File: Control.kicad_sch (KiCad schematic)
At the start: 8 parts, among them U1 XC95144XL-TQ100

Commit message: more
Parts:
- removed U1: XC95144XL-TQ100, stdpads:TQFP-100_14x14mm_P0.5mm, symbol CPLD_Xilinx:XC95144XL-TQ100
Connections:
- no-connect marks 2 -> 0

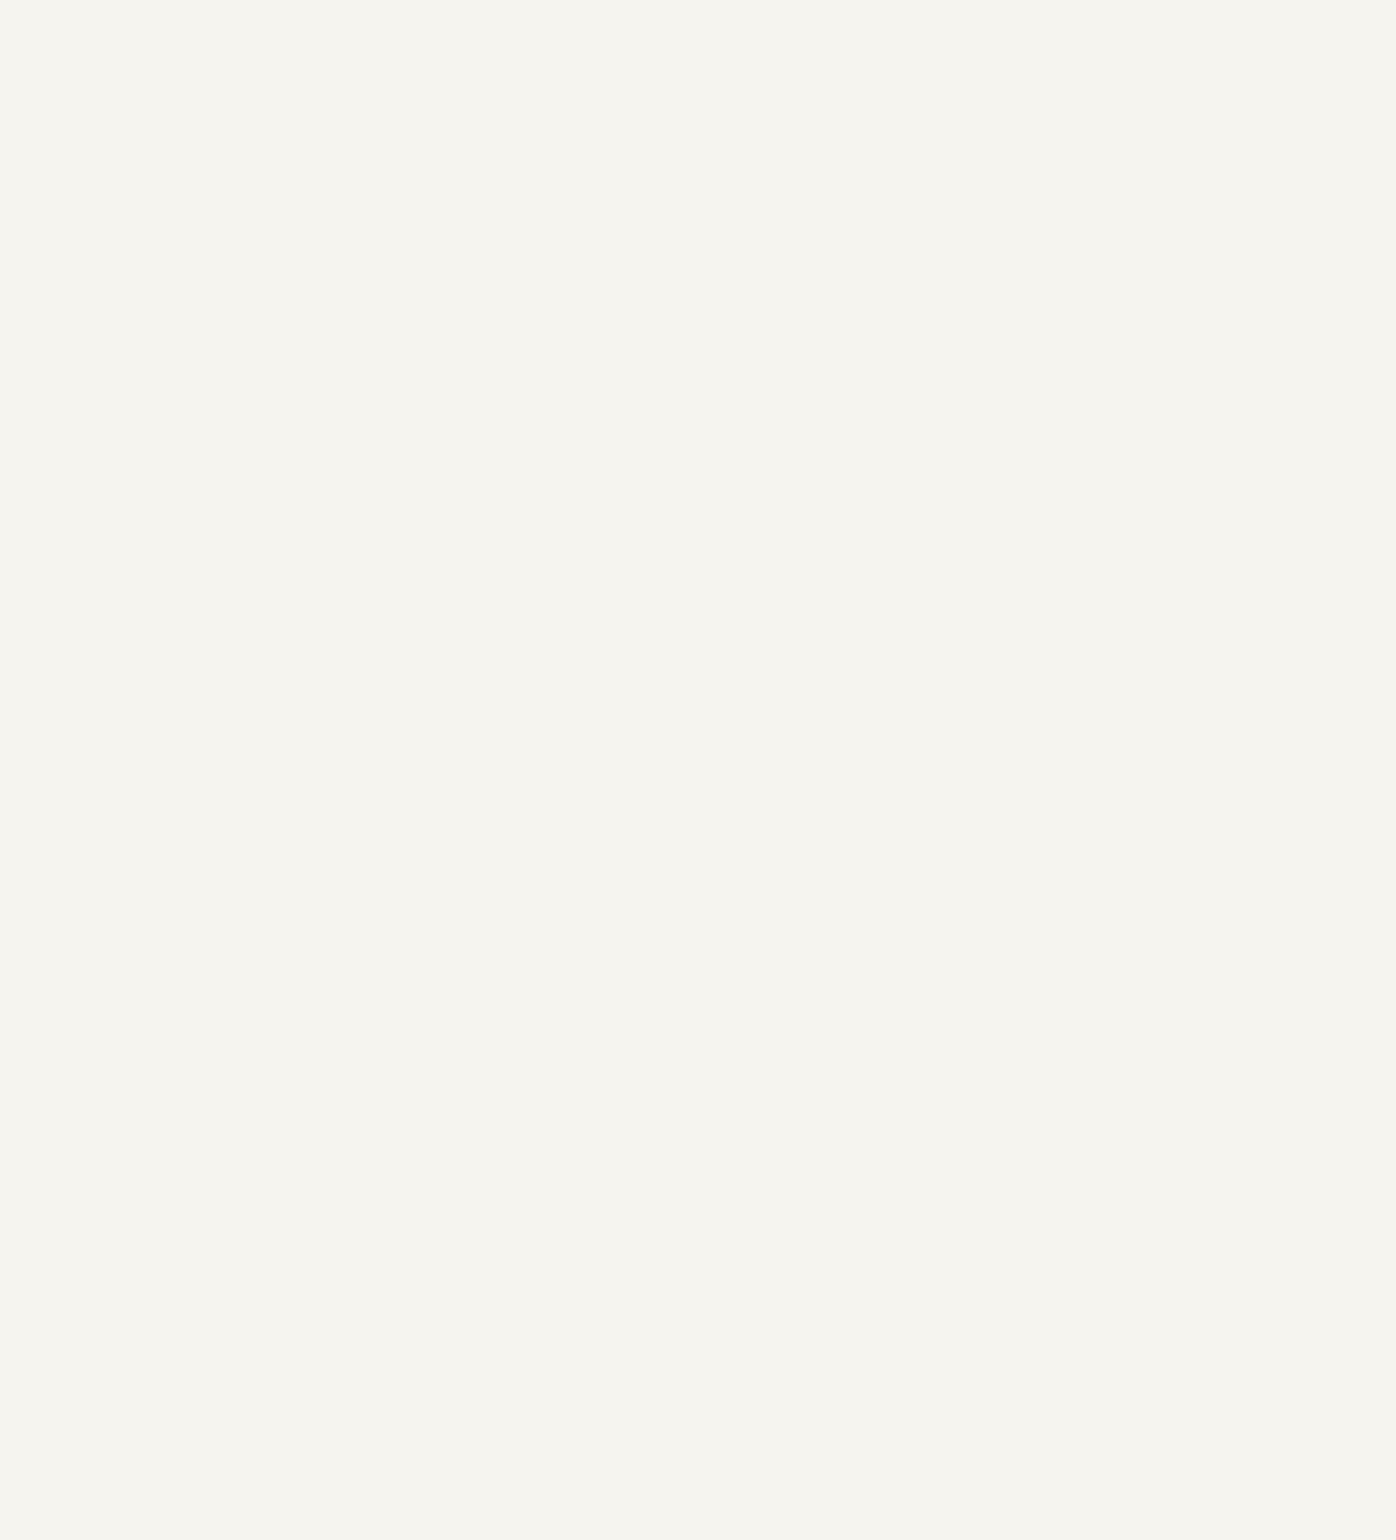
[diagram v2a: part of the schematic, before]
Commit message: better PDS muxing
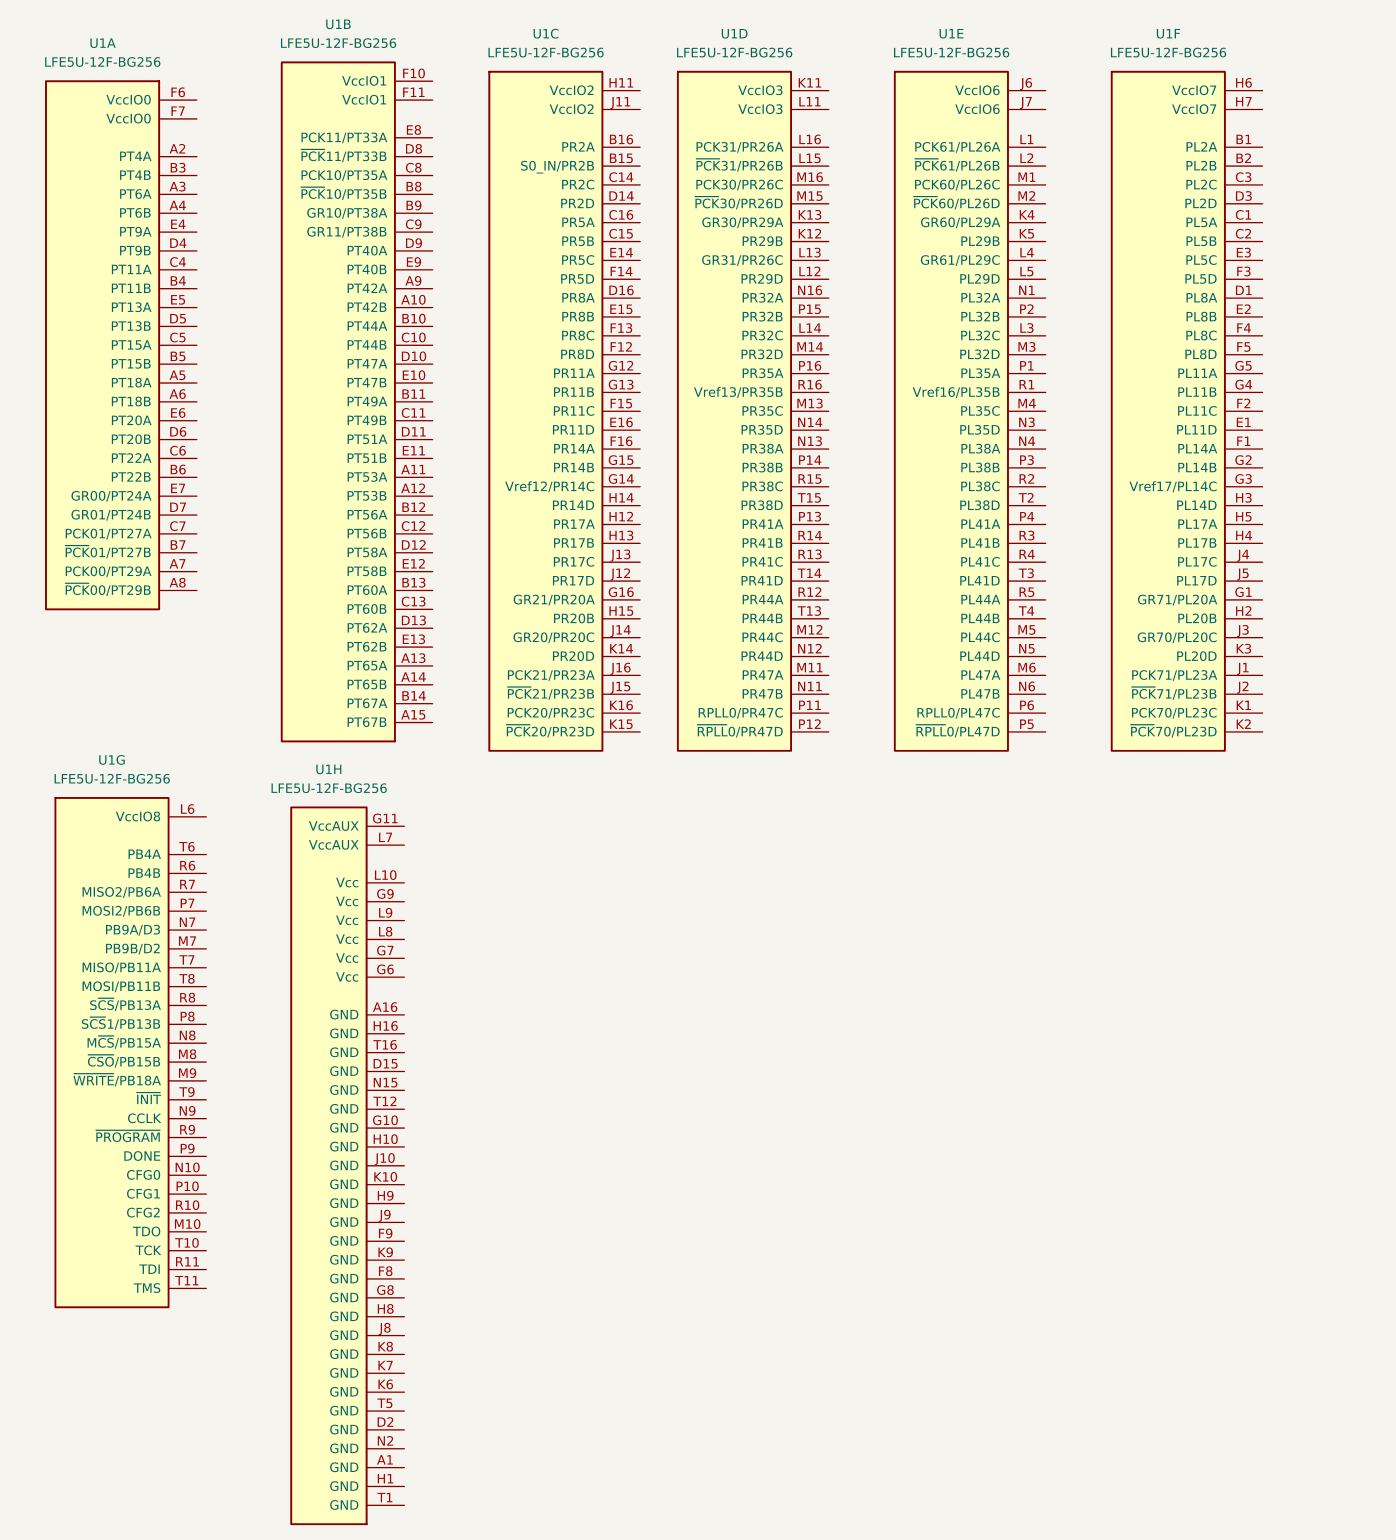
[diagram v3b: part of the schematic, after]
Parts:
- added U1: LFE5U-12F-BG256, stdpads:Lattice_CABGA-256, symbol GW_PLD:LFE5U-12F-BG256
